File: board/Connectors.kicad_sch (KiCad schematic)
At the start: 8 parts, among them J10 Bus_Hydra_8bit, J11 Bus_Hydra_8bit, J12 Bus_Hydra_8bit, J13 Bus_Hydra_8bit, J14 Bus_Hydra_8bit, J15 Bus_Hydra_8bit, J16 Bus_Hydra_8bit, J9 Bus_Hydra_8bit

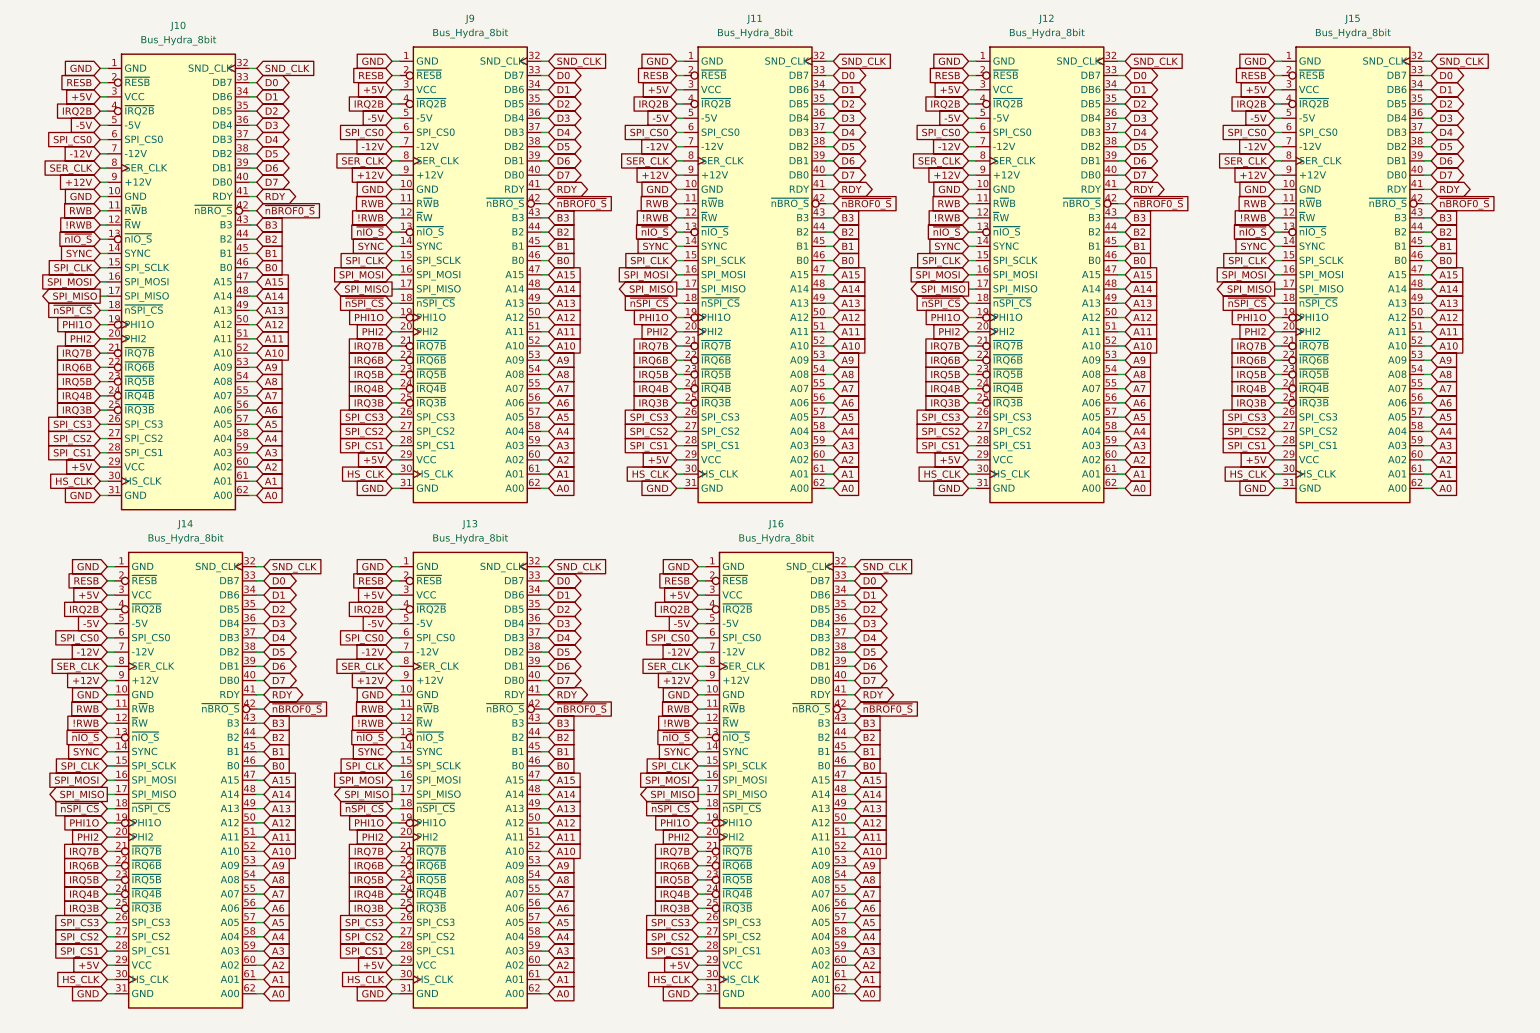
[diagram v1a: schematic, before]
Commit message: Added surface mount version of memory daughter cards, and lots of schematic updates and fixes, including adding dedicated registers for shared memory bank select at $FFF1 and IRQ vTable entry selector at $FFF2 along with the IRQ vTable registers and priority encoders for 16 IRQs
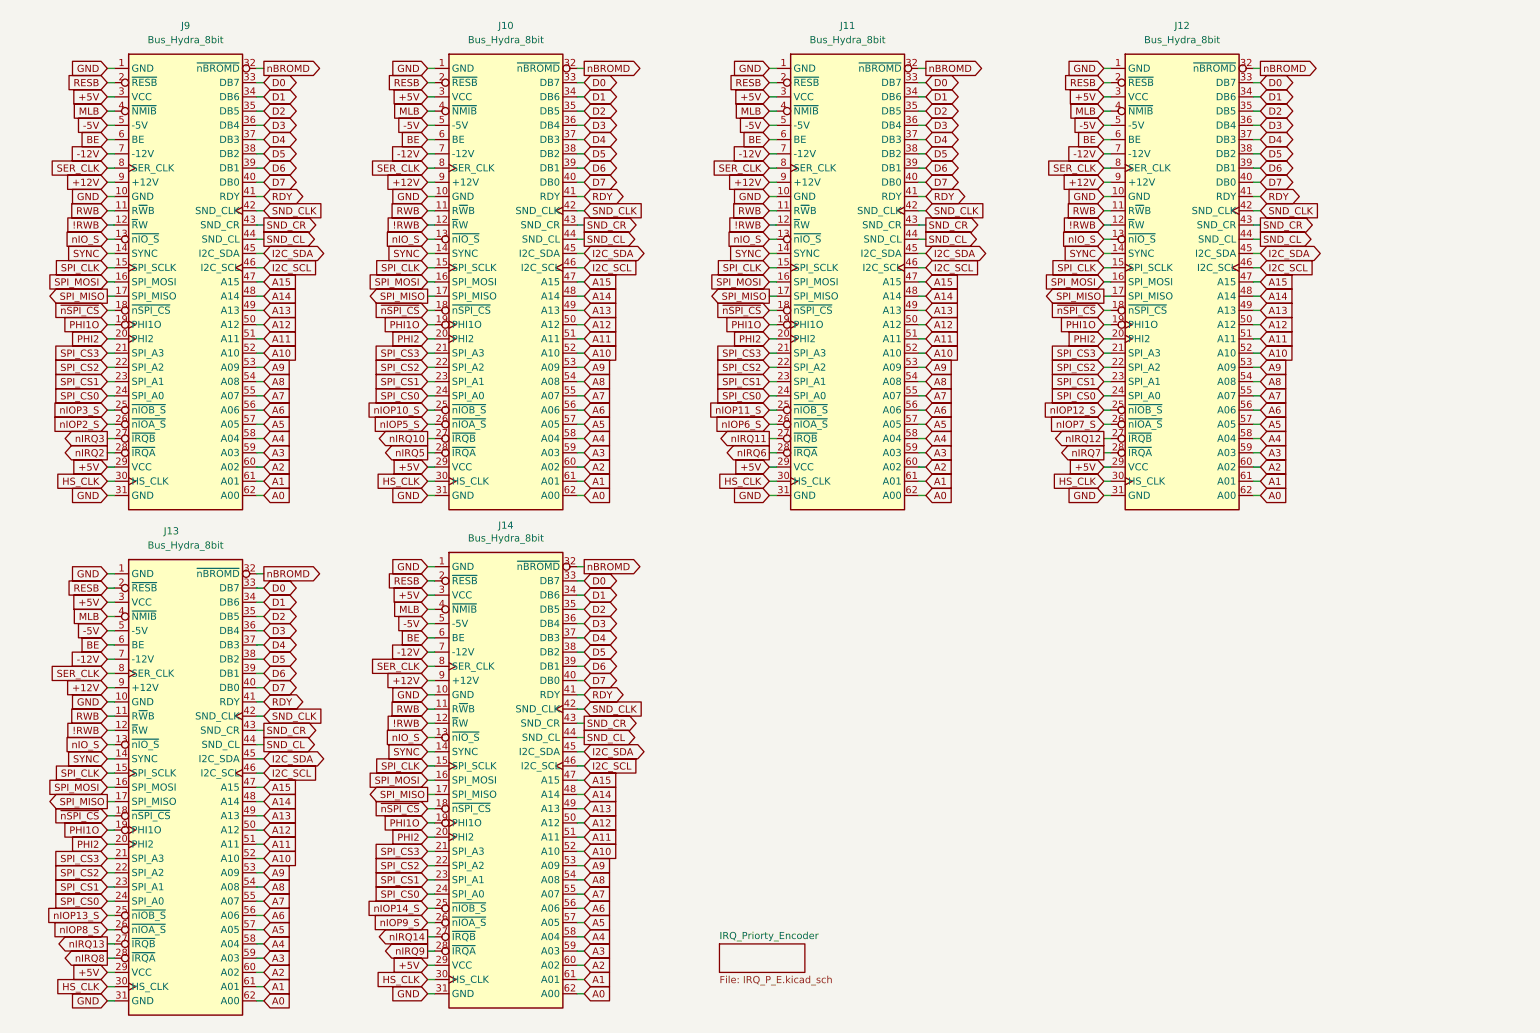
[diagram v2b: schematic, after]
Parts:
- removed J15, J16: Bus_Hydra_8bit, PC Edge:TE_7-5530843-0, symbol Connector:Bus_Hydra_8bit
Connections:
- net IRQ4B is gone; now on net SPI_CS0: J10.24 (SPI_A0), J11.24 (SPI_A0), J12.24 (SPI_A0), J13.24 (SPI_A0), J14.24 (SPI_A0), J9.24 (SPI_A0)
- net IRQ5B is gone; now on net SPI_CS1: J10.23 (SPI_A1), J11.23 (SPI_A1), J12.23 (SPI_A1), J13.23 (SPI_A1), J14.23 (SPI_A1), J9.23 (SPI_A1)
- net IRQ6B is gone; now on net SPI_CS2: J10.22 (SPI_A2), J11.22 (SPI_A2), J12.22 (SPI_A2), J13.22 (SPI_A2), J14.22 (SPI_A2), J9.22 (SPI_A2)
- net IRQ7B is gone; now on net SPI_CS3: J10.21 (SPI_A3), J11.21 (SPI_A3), J12.21 (SPI_A3), J13.21 (SPI_A3), J14.21 (SPI_A3), J9.21 (SPI_A3)
- net ~{nBROF0_S} is gone; now on net SND_CLK: J10.42 (SND_CLK), J11.42 (SND_CLK), J12.42 (SND_CLK), J13.42 (SND_CLK), J14.42 (SND_CLK), J9.42 (SND_CLK)
- net SND_CLK: no longer J10.32 (SND_CLK), J11.32 (SND_CLK), J12.32 (SND_CLK), J13.32 (SND_CLK), J14.32 (SND_CLK), J9.32 (SND_CLK)
- net SPI_CS0: no longer J10.6 (SPI_CS0), J11.6 (SPI_CS0), J12.6 (SPI_CS0), J13.6 (SPI_CS0), J14.6 (SPI_CS0), J9.6 (SPI_CS0)
- net SPI_CS1: no longer J10.28 (SPI_CS1), J11.28 (SPI_CS1), J12.28 (SPI_CS1), J13.28 (SPI_CS1), J14.28 (SPI_CS1), J9.28 (SPI_CS1)
- net SPI_CS2: no longer J10.27 (SPI_CS2), J11.27 (SPI_CS2), J12.27 (SPI_CS2), J13.27 (SPI_CS2), J14.27 (SPI_CS2), J9.27 (SPI_CS2)
- net SPI_CS3: no longer J10.26 (SPI_CS3), J11.26 (SPI_CS3), J12.26 (SPI_CS3), J13.26 (SPI_CS3), J14.26 (SPI_CS3), J9.26 (SPI_CS3)
- net B0 renamed I2C_SCL
- net B1 renamed I2C_SDA
- net B2 renamed SND_CL
- net B3 renamed SND_CR
- net IRQ2B renamed MLB
- removed net IRQ3B: J10.25 (~{IRQ3B}), J11.25 (~{IRQ3B}), J12.25 (~{IRQ3B}), J13.25 (~{IRQ3B}), J14.25 (~{IRQ3B}), J9.25 (~{IRQ3B})
- net ~{nIO_S} renamed nIO_S
- new net BE: J10.6 (BE), J11.6 (BE), J12.6 (BE), J13.6 (BE), J14.6 (BE), J9.6 (BE)
- new net nBROMD: J10.32 (~{nBROMD}), J11.32 (~{nBROMD}), J12.32 (~{nBROMD}), J13.32 (~{nBROMD}), J14.32 (~{nBROMD}), J9.32 (~{nBROMD})
- new net nIOP10_S: J10.25 (~{nIOB_S})
- new net nIOP11_S: J11.25 (~{nIOB_S})
- new net nIOP12_S: J12.25 (~{nIOB_S})
- new net nIOP13_S: J13.25 (~{nIOB_S})
- new net nIOP14_S: J14.25 (~{nIOB_S})
- new net nIOP2_S: J9.26 (~{nIOA_S})
- new net nIOP3_S: J9.25 (~{nIOB_S})
- new net nIOP5_S: J10.26 (~{nIOA_S})
- new net nIOP6_S: J11.26 (~{nIOA_S})
- new net nIOP7_S: J12.26 (~{nIOA_S})
- new net nIOP8_S: J13.26 (~{nIOA_S})
- new net nIOP9_S: J14.26 (~{nIOA_S})
- new net nIRQ10: J10.27 (~{IRQB})
- new net nIRQ11: J11.27 (~{IRQB})
- new net nIRQ12: J12.27 (~{IRQB})
- new net nIRQ13: J13.27 (~{IRQB})
- new net nIRQ14: J14.27 (~{IRQB})
- new net nIRQ2: J9.28 (~{IRQA})
- new net nIRQ3: J9.27 (~{IRQB})
- new net nIRQ5: J10.28 (~{IRQA})
- new net nIRQ6: J11.28 (~{IRQA})
- new net nIRQ7: J12.28 (~{IRQA})
- new net nIRQ8: J13.28 (~{IRQA})
- new net nIRQ9: J14.28 (~{IRQA})
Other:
- added sheet IRQ_Priorty_Encoder (IRQ_P_E.kicad_sch)

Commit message: More main PCB updates.  Rearranged some things.  Bypass caps near PS connector.  Moved front panel connector to opposite side of board.
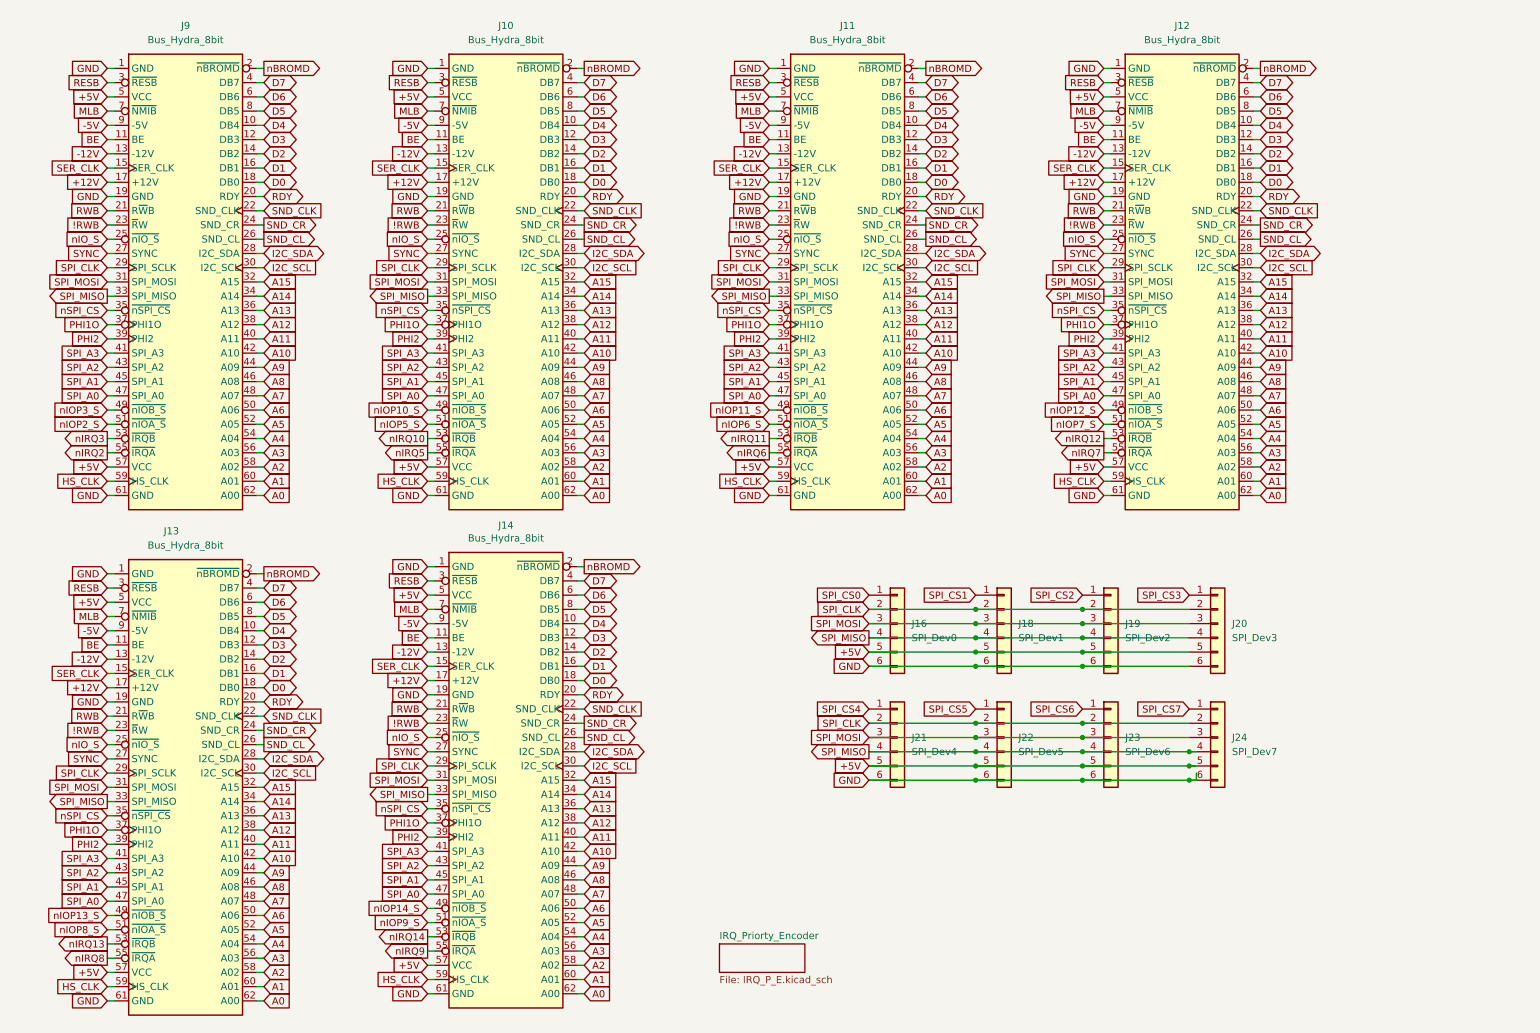
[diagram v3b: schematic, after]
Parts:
- added J16: SPI_Dev0, Connector_PinSocket_2.54mm:PinSocket_1x06_P2.54mm_Vertical, symbol Connector_Generic:Conn_01x06
- added J18: SPI_Dev1, Connector_PinSocket_2.54mm:PinSocket_1x06_P2.54mm_Vertical, symbol Connector_Generic:Conn_01x06
- added J19: SPI_Dev2, Connector_PinSocket_2.54mm:PinSocket_1x06_P2.54mm_Vertical, symbol Connector_Generic:Conn_01x06
- added J20: SPI_Dev3, Connector_PinSocket_2.54mm:PinSocket_1x06_P2.54mm_Vertical, symbol Connector_Generic:Conn_01x06
- added J21: SPI_Dev4, Connector_PinSocket_2.54mm:PinSocket_1x06_P2.54mm_Vertical, symbol Connector_Generic:Conn_01x06
- added J22: SPI_Dev5, Connector_PinSocket_2.54mm:PinSocket_1x06_P2.54mm_Vertical, symbol Connector_Generic:Conn_01x06
- added J23: SPI_Dev6, Connector_PinSocket_2.54mm:PinSocket_1x06_P2.54mm_Vertical, symbol Connector_Generic:Conn_01x06
- added J24: SPI_Dev7, Connector_PinSocket_2.54mm:PinSocket_1x06_P2.54mm_Vertical, symbol Connector_Generic:Conn_01x06
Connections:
- net ~{nSPI_CS} is gone; now on net D0: J10.18 (DB0), J11.18 (DB0), J12.18 (DB0), J13.18 (DB0), J14.18 (DB0), J9.18 (DB0)
- net !RWB: now also J10.23 (~{R}W), J11.23 (~{R}W), J12.23 (~{R}W), J13.23 (~{R}W), J14.23 (~{R}W), J9.23 (~{R}W); no longer J10.12 (~{R}W), J11.12 (~{R}W), J12.12 (~{R}W), J13.12 (~{R}W), J14.12 (~{R}W), J9.12 (~{R}W)
- net +12V: now also J10.17 (+12V), J11.17 (+12V), J12.17 (+12V), J13.17 (+12V), J14.17 (+12V), J9.17 (+12V); no longer J10.9 (+12V), J11.9 (+12V), J12.9 (+12V), J13.9 (+12V), J14.9 (+12V), J9.9 (+12V)
- net +5V: now also J10.5 (VCC), J10.57 (VCC), J11.5 (VCC), J11.57 (VCC), J12.5 (VCC), J12.57 (VCC), J13.5 (VCC), J13.57 (VCC), J14.5 (VCC), J14.57 (VCC), J9.5 (VCC), J9.57 (VCC), J16.5 (Pin_5), J18.5 (Pin_5), J19.5 (Pin_5), J20.5 (Pin_5), J21.5 (Pin_5), J22.5 (Pin_5), J23.5 (Pin_5), J24.5 (Pin_5); no longer J10.29 (VCC), J10.3 (VCC), J11.29 (VCC), J11.3 (VCC), J12.29 (VCC), J12.3 (VCC), J13.29 (VCC), J13.3 (VCC), J14.29 (VCC), J14.3 (VCC), J9.29 (VCC), J9.3 (VCC)
- net -12V: now also J10.13 (-12V), J11.13 (-12V), J12.13 (-12V), J13.13 (-12V), J14.13 (-12V), J9.13 (-12V); no longer J10.7 (-12V), J11.7 (-12V), J12.7 (-12V), J13.7 (-12V), J14.7 (-12V), J9.7 (-12V)
- net -5V: now also J10.9 (-5V), J11.9 (-5V), J12.9 (-5V), J13.9 (-5V), J14.9 (-5V), J9.9 (-5V); no longer J10.5 (-5V), J11.5 (-5V), J12.5 (-5V), J13.5 (-5V), J14.5 (-5V), J9.5 (-5V)
- net A1: now also J10.60 (A01), J11.60 (A01), J12.60 (A01), J13.60 (A01), J14.60 (A01), J9.60 (A01); no longer J10.61 (A01), J11.61 (A01), J12.61 (A01), J13.61 (A01), J14.61 (A01), J9.61 (A01)
- net A10: now also J10.42 (A10), J11.42 (A10), J12.42 (A10), J13.42 (A10), J14.42 (A10), J9.42 (A10); no longer J10.52 (A10), J11.52 (A10), J12.52 (A10), J13.52 (A10), J14.52 (A10), J9.52 (A10)
- net A11: now also J10.40 (A11), J11.40 (A11), J12.40 (A11), J13.40 (A11), J14.40 (A11), J9.40 (A11); no longer J10.51 (A11), J11.51 (A11), J12.51 (A11), J13.51 (A11), J14.51 (A11), J9.51 (A11)
- net A12: now also J10.38 (A12), J11.38 (A12), J12.38 (A12), J13.38 (A12), J14.38 (A12), J9.38 (A12); no longer J10.50 (A12), J11.50 (A12), J12.50 (A12), J13.50 (A12), J14.50 (A12), J9.50 (A12)
- net A13: now also J10.36 (A13), J11.36 (A13), J12.36 (A13), J13.36 (A13), J14.36 (A13), J9.36 (A13); no longer J10.49 (A13), J11.49 (A13), J12.49 (A13), J13.49 (A13), J14.49 (A13), J9.49 (A13)
- net A14: now also J10.34 (A14), J11.34 (A14), J12.34 (A14), J13.34 (A14), J14.34 (A14), J9.34 (A14); no longer J10.48 (A14), J11.48 (A14), J12.48 (A14), J13.48 (A14), J14.48 (A14), J9.48 (A14)
- net A15: now also J10.32 (A15), J11.32 (A15), J12.32 (A15), J13.32 (A15), J14.32 (A15), J9.32 (A15); no longer J10.47 (A15), J11.47 (A15), J12.47 (A15), J13.47 (A15), J14.47 (A15), J9.47 (A15)
- net A2: now also J10.58 (A02), J11.58 (A02), J12.58 (A02), J13.58 (A02), J14.58 (A02), J9.58 (A02); no longer J10.60 (A02), J11.60 (A02), J12.60 (A02), J13.60 (A02), J14.60 (A02), J9.60 (A02)
- net A3: now also J10.56 (A03), J11.56 (A03), J12.56 (A03), J13.56 (A03), J14.56 (A03), J9.56 (A03); no longer J10.59 (A03), J11.59 (A03), J12.59 (A03), J13.59 (A03), J14.59 (A03), J9.59 (A03)
- net A4: now also J10.54 (A04), J11.54 (A04), J12.54 (A04), J13.54 (A04), J14.54 (A04), J9.54 (A04); no longer J10.58 (A04), J11.58 (A04), J12.58 (A04), J13.58 (A04), J14.58 (A04), J9.58 (A04)
- net A5: now also J10.52 (A05), J11.52 (A05), J12.52 (A05), J13.52 (A05), J14.52 (A05), J9.52 (A05); no longer J10.57 (A05), J11.57 (A05), J12.57 (A05), J13.57 (A05), J14.57 (A05), J9.57 (A05)
- net A6: now also J10.50 (A06), J11.50 (A06), J12.50 (A06), J13.50 (A06), J14.50 (A06), J9.50 (A06); no longer J10.56 (A06), J11.56 (A06), J12.56 (A06), J13.56 (A06), J14.56 (A06), J9.56 (A06)
- net A7: now also J10.48 (A07), J11.48 (A07), J12.48 (A07), J13.48 (A07), J14.48 (A07), J9.48 (A07); no longer J10.55 (A07), J11.55 (A07), J12.55 (A07), J13.55 (A07), J14.55 (A07), J9.55 (A07)
- net A8: now also J10.46 (A08), J11.46 (A08), J12.46 (A08), J13.46 (A08), J14.46 (A08), J9.46 (A08); no longer J10.54 (A08), J11.54 (A08), J12.54 (A08), J13.54 (A08), J14.54 (A08), J9.54 (A08)
- net A9: now also J10.44 (A09), J11.44 (A09), J12.44 (A09), J13.44 (A09), J14.44 (A09), J9.44 (A09); no longer J10.53 (A09), J11.53 (A09), J12.53 (A09), J13.53 (A09), J14.53 (A09), J9.53 (A09)
- net BE: now also J10.11 (BE), J11.11 (BE), J12.11 (BE), J13.11 (BE), J14.11 (BE), J9.11 (BE); no longer J10.6 (BE), J11.6 (BE), J12.6 (BE), J13.6 (BE), J14.6 (BE), J9.6 (BE)
- net D0: no longer J10.33 (DB7), J11.33 (DB7), J12.33 (DB7), J13.33 (DB7), J14.33 (DB7), J9.33 (DB7)
- net D1: now also J10.16 (DB1), J11.16 (DB1), J12.16 (DB1), J13.16 (DB1), J14.16 (DB1), J9.16 (DB1); no longer J10.34 (DB6), J11.34 (DB6), J12.34 (DB6), J13.34 (DB6), J14.34 (DB6), J9.34 (DB6)
- net D2: now also J10.14 (DB2), J11.14 (DB2), J12.14 (DB2), J13.14 (DB2), J14.14 (DB2), J9.14 (DB2); no longer J10.35 (DB5), J11.35 (DB5), J12.35 (DB5), J13.35 (DB5), J14.35 (DB5), J9.35 (DB5)
- net D3: now also J10.12 (DB3), J11.12 (DB3), J12.12 (DB3), J13.12 (DB3), J14.12 (DB3), J9.12 (DB3); no longer J10.36 (DB4), J11.36 (DB4), J12.36 (DB4), J13.36 (DB4), J14.36 (DB4), J9.36 (DB4)
- net D4: now also J10.10 (DB4), J11.10 (DB4), J12.10 (DB4), J13.10 (DB4), J14.10 (DB4), J9.10 (DB4); no longer J10.37 (DB3), J11.37 (DB3), J12.37 (DB3), J13.37 (DB3), J14.37 (DB3), J9.37 (DB3)
- net D5: now also J10.8 (DB5), J11.8 (DB5), J12.8 (DB5), J13.8 (DB5), J14.8 (DB5), J9.8 (DB5); no longer J10.38 (DB2), J11.38 (DB2), J12.38 (DB2), J13.38 (DB2), J14.38 (DB2), J9.38 (DB2)
- net D6: now also J10.6 (DB6), J11.6 (DB6), J12.6 (DB6), J13.6 (DB6), J14.6 (DB6), J9.6 (DB6); no longer J10.39 (DB1), J11.39 (DB1), J12.39 (DB1), J13.39 (DB1), J14.39 (DB1), J9.39 (DB1)
- net D7: now also J10.4 (DB7), J11.4 (DB7), J12.4 (DB7), J13.4 (DB7), J14.4 (DB7), J9.4 (DB7); no longer J10.40 (DB0), J11.40 (DB0), J12.40 (DB0), J13.40 (DB0), J14.40 (DB0), J9.40 (DB0)
- net GND: now also J10.19 (GND), J10.61 (GND), J11.19 (GND), J11.61 (GND), J12.19 (GND), J12.61 (GND), J13.19 (GND), J13.61 (GND), J14.19 (GND), J14.61 (GND), J9.19 (GND), J9.61 (GND), J16.6 (Pin_6), J18.6 (Pin_6), J19.6 (Pin_6), J20.6 (Pin_6), J21.6 (Pin_6), J22.6 (Pin_6), J23.6 (Pin_6), J24.6 (Pin_6); no longer J10.10 (GND), J10.31 (GND), J11.10 (GND), J11.31 (GND), J12.10 (GND), J12.31 (GND), J13.10 (GND), J13.31 (GND), J14.10 (GND), J14.31 (GND), J9.10 (GND), J9.31 (GND)
- net HS_CLK: now also J10.59 (HS_CLK), J11.59 (HS_CLK), J12.59 (HS_CLK), J13.59 (HS_CLK), J14.59 (HS_CLK), J9.59 (HS_CLK); no longer J10.30 (HS_CLK), J11.30 (HS_CLK), J12.30 (HS_CLK), J13.30 (HS_CLK), J14.30 (HS_CLK), J9.30 (HS_CLK)
- net I2C_SCL: now also J10.30 (I2C_SCL), J11.30 (I2C_SCL), J12.30 (I2C_SCL), J13.30 (I2C_SCL), J14.30 (I2C_SCL), J9.30 (I2C_SCL); no longer J10.46 (I2C_SCL), J11.46 (I2C_SCL), J12.46 (I2C_SCL), J13.46 (I2C_SCL), J14.46 (I2C_SCL), J9.46 (I2C_SCL)
- net I2C_SDA: now also J10.28 (I2C_SDA), J11.28 (I2C_SDA), J12.28 (I2C_SDA), J13.28 (I2C_SDA), J14.28 (I2C_SDA), J9.28 (I2C_SDA); no longer J10.45 (I2C_SDA), J11.45 (I2C_SDA), J12.45 (I2C_SDA), J13.45 (I2C_SDA), J14.45 (I2C_SDA), J9.45 (I2C_SDA)
- net MLB: now also J10.7 (~{NMIB}), J11.7 (~{NMIB}), J12.7 (~{NMIB}), J13.7 (~{NMIB}), J14.7 (~{NMIB}), J9.7 (~{NMIB}); no longer J10.4 (~{NMIB}), J11.4 (~{NMIB}), J12.4 (~{NMIB}), J13.4 (~{NMIB}), J14.4 (~{NMIB}), J9.4 (~{NMIB})
- net PHI1O: now also J10.37 (PHI1O), J11.37 (PHI1O), J12.37 (PHI1O), J13.37 (PHI1O), J14.37 (PHI1O), J9.37 (PHI1O); no longer J10.19 (PHI1O), J11.19 (PHI1O), J12.19 (PHI1O), J13.19 (PHI1O), J14.19 (PHI1O), J9.19 (PHI1O)
- net PHI2: now also J10.39 (PHI2), J11.39 (PHI2), J12.39 (PHI2), J13.39 (PHI2), J14.39 (PHI2), J9.39 (PHI2); no longer J10.20 (PHI2), J11.20 (PHI2), J12.20 (PHI2), J13.20 (PHI2), J14.20 (PHI2), J9.20 (PHI2)
- net RDY: now also J10.20 (RDY), J11.20 (RDY), J12.20 (RDY), J13.20 (RDY), J14.20 (RDY), J9.20 (RDY); no longer J10.41 (RDY), J11.41 (RDY), J12.41 (RDY), J13.41 (RDY), J14.41 (RDY), J9.41 (RDY)
- net RESB: now also J10.3 (~{RESB}), J11.3 (~{RESB}), J12.3 (~{RESB}), J13.3 (~{RESB}), J14.3 (~{RESB}), J9.3 (~{RESB}); no longer J10.2 (~{RESB}), J11.2 (~{RESB}), J12.2 (~{RESB}), J13.2 (~{RESB}), J14.2 (~{RESB}), J9.2 (~{RESB})
- net RWB: now also J10.21 (R~{W}B), J11.21 (R~{W}B), J12.21 (R~{W}B), J13.21 (R~{W}B), J14.21 (R~{W}B), J9.21 (R~{W}B); no longer J10.11 (R~{W}B), J11.11 (R~{W}B), J12.11 (R~{W}B), J13.11 (R~{W}B), J14.11 (R~{W}B), J9.11 (R~{W}B)
- net SER_CLK: now also J10.15 (SER_CLK), J11.15 (SER_CLK), J12.15 (SER_CLK), J13.15 (SER_CLK), J14.15 (SER_CLK), J9.15 (SER_CLK); no longer J10.8 (SER_CLK), J11.8 (SER_CLK), J12.8 (SER_CLK), J13.8 (SER_CLK), J14.8 (SER_CLK), J9.8 (SER_CLK)
- net SND_CL: now also J10.26 (SND_CL), J11.26 (SND_CL), J12.26 (SND_CL), J13.26 (SND_CL), J14.26 (SND_CL), J9.26 (SND_CL); no longer J10.44 (SND_CL), J11.44 (SND_CL), J12.44 (SND_CL), J13.44 (SND_CL), J14.44 (SND_CL), J9.44 (SND_CL)
- net SND_CLK: now also J10.22 (SND_CLK), J11.22 (SND_CLK), J12.22 (SND_CLK), J13.22 (SND_CLK), J14.22 (SND_CLK), J9.22 (SND_CLK); no longer J10.42 (SND_CLK), J11.42 (SND_CLK), J12.42 (SND_CLK), J13.42 (SND_CLK), J14.42 (SND_CLK), J9.42 (SND_CLK)
- net SND_CR: now also J10.24 (SND_CR), J11.24 (SND_CR), J12.24 (SND_CR), J13.24 (SND_CR), J14.24 (SND_CR), J9.24 (SND_CR); no longer J10.43 (SND_CR), J11.43 (SND_CR), J12.43 (SND_CR), J13.43 (SND_CR), J14.43 (SND_CR), J9.43 (SND_CR)
- net SPI_CLK: now also J10.29 (SPI_SCLK), J11.29 (SPI_SCLK), J12.29 (SPI_SCLK), J13.29 (SPI_SCLK), J14.29 (SPI_SCLK), J9.29 (SPI_SCLK), J16.2 (Pin_2), J18.2 (Pin_2), J19.2 (Pin_2), J20.2 (Pin_2), J21.2 (Pin_2), J22.2 (Pin_2), J23.2 (Pin_2), J24.2 (Pin_2); no longer J10.15 (SPI_SCLK), J11.15 (SPI_SCLK), J12.15 (SPI_SCLK), J13.15 (SPI_SCLK), J14.15 (SPI_SCLK), J9.15 (SPI_SCLK)
- net SPI_CS0: now also J16.1 (Pin_1); no longer J10.24 (SPI_A0), J11.24 (SPI_A0), J12.24 (SPI_A0), J13.24 (SPI_A0), J14.24 (SPI_A0), J9.24 (SPI_A0)
- net SPI_CS1: now also J18.1 (Pin_1); no longer J10.23 (SPI_A1), J11.23 (SPI_A1), J12.23 (SPI_A1), J13.23 (SPI_A1), J14.23 (SPI_A1), J9.23 (SPI_A1)
- net SPI_CS2: now also J19.1 (Pin_1); no longer J10.22 (SPI_A2), J11.22 (SPI_A2), J12.22 (SPI_A2), J13.22 (SPI_A2), J14.22 (SPI_A2), J9.22 (SPI_A2)
- net SPI_CS3: now also J20.1 (Pin_1); no longer J10.21 (SPI_A3), J11.21 (SPI_A3), J12.21 (SPI_A3), J13.21 (SPI_A3), J14.21 (SPI_A3), J9.21 (SPI_A3)
- net SPI_MISO: now also J10.33 (SPI_MISO), J11.33 (SPI_MISO), J12.33 (SPI_MISO), J13.33 (SPI_MISO), J14.33 (SPI_MISO), J9.33 (SPI_MISO), J16.4 (Pin_4), J18.4 (Pin_4), J19.4 (Pin_4), J20.4 (Pin_4), J21.4 (Pin_4), J22.4 (Pin_4), J23.4 (Pin_4), J24.4 (Pin_4); no longer J10.17 (SPI_MISO), J11.17 (SPI_MISO), J12.17 (SPI_MISO), J13.17 (SPI_MISO), J14.17 (SPI_MISO), J9.17 (SPI_MISO)
- net SPI_MOSI: now also J10.31 (SPI_MOSI), J11.31 (SPI_MOSI), J12.31 (SPI_MOSI), J13.31 (SPI_MOSI), J14.31 (SPI_MOSI), J9.31 (SPI_MOSI), J16.3 (Pin_3), J18.3 (Pin_3), J19.3 (Pin_3), J20.3 (Pin_3), J21.3 (Pin_3), J22.3 (Pin_3), J23.3 (Pin_3), J24.3 (Pin_3); no longer J10.16 (SPI_MOSI), J11.16 (SPI_MOSI), J12.16 (SPI_MOSI), J13.16 (SPI_MOSI), J14.16 (SPI_MOSI), J9.16 (SPI_MOSI)
- net SYNC: now also J10.27 (SYNC), J11.27 (SYNC), J12.27 (SYNC), J13.27 (SYNC), J14.27 (SYNC), J9.27 (SYNC); no longer J10.14 (SYNC), J11.14 (SYNC), J12.14 (SYNC), J13.14 (SYNC), J14.14 (SYNC), J9.14 (SYNC)
- net nBROMD: now also J10.2 (~{nBROMD}), J11.2 (~{nBROMD}), J12.2 (~{nBROMD}), J13.2 (~{nBROMD}), J14.2 (~{nBROMD}), J9.2 (~{nBROMD}); no longer J10.32 (~{nBROMD}), J11.32 (~{nBROMD}), J12.32 (~{nBROMD}), J13.32 (~{nBROMD}), J14.32 (~{nBROMD}), J9.32 (~{nBROMD})
- net nIOP10_S: now also J10.49 (~{nIOB_S}); no longer J10.25 (~{nIOB_S})
- net nIOP11_S: now also J11.49 (~{nIOB_S}); no longer J11.25 (~{nIOB_S})
- net nIOP12_S: now also J12.49 (~{nIOB_S}); no longer J12.25 (~{nIOB_S})
- net nIOP13_S: now also J13.49 (~{nIOB_S}); no longer J13.25 (~{nIOB_S})
- net nIOP14_S: now also J14.49 (~{nIOB_S}); no longer J14.25 (~{nIOB_S})
- net nIOP2_S: now also J9.51 (~{nIOA_S}); no longer J9.26 (~{nIOA_S})
- net nIOP3_S: now also J9.49 (~{nIOB_S}); no longer J9.25 (~{nIOB_S})
- net nIOP5_S: now also J10.51 (~{nIOA_S}); no longer J10.26 (~{nIOA_S})
- net nIOP6_S: now also J11.51 (~{nIOA_S}); no longer J11.26 (~{nIOA_S})
- net nIOP7_S: now also J12.51 (~{nIOA_S}); no longer J12.26 (~{nIOA_S})
- net nIOP8_S: now also J13.51 (~{nIOA_S}); no longer J13.26 (~{nIOA_S})
- net nIOP9_S: now also J14.51 (~{nIOA_S}); no longer J14.26 (~{nIOA_S})
- net nIO_S: now also J10.25 (~{nIO_S}), J11.25 (~{nIO_S}), J12.25 (~{nIO_S}), J13.25 (~{nIO_S}), J14.25 (~{nIO_S}), J9.25 (~{nIO_S}); no longer J10.13 (~{nIO_S}), J11.13 (~{nIO_S}), J12.13 (~{nIO_S}), J13.13 (~{nIO_S}), J14.13 (~{nIO_S}), J9.13 (~{nIO_S})
- net nIRQ10: now also J10.53 (~{IRQB}); no longer J10.27 (~{IRQB})
- net nIRQ11: now also J11.53 (~{IRQB}); no longer J11.27 (~{IRQB})
- net nIRQ12: now also J12.53 (~{IRQB}); no longer J12.27 (~{IRQB})
- net nIRQ13: now also J13.53 (~{IRQB}); no longer J13.27 (~{IRQB})
- net nIRQ14: now also J14.53 (~{IRQB}); no longer J14.27 (~{IRQB})
- net nIRQ2: now also J9.55 (~{IRQA}); no longer J9.28 (~{IRQA})
- net nIRQ3: now also J9.53 (~{IRQB}); no longer J9.27 (~{IRQB})
- net nIRQ5: now also J10.55 (~{IRQA}); no longer J10.28 (~{IRQA})
- net nIRQ6: now also J11.55 (~{IRQA}); no longer J11.28 (~{IRQA})
- net nIRQ7: now also J12.55 (~{IRQA}); no longer J12.28 (~{IRQA})
- net nIRQ8: now also J13.55 (~{IRQA}); no longer J13.28 (~{IRQA})
- net nIRQ9: now also J14.55 (~{IRQA}); no longer J14.28 (~{IRQA})
- new net SPI_A0: J10.47 (SPI_A0), J11.47 (SPI_A0), J12.47 (SPI_A0), J13.47 (SPI_A0), J14.47 (SPI_A0), J9.47 (SPI_A0)
- new net SPI_A1: J10.45 (SPI_A1), J11.45 (SPI_A1), J12.45 (SPI_A1), J13.45 (SPI_A1), J14.45 (SPI_A1), J9.45 (SPI_A1)
- new net SPI_A2: J10.43 (SPI_A2), J11.43 (SPI_A2), J12.43 (SPI_A2), J13.43 (SPI_A2), J14.43 (SPI_A2), J9.43 (SPI_A2)
- new net SPI_A3: J10.41 (SPI_A3), J11.41 (SPI_A3), J12.41 (SPI_A3), J13.41 (SPI_A3), J14.41 (SPI_A3), J9.41 (SPI_A3)
- new net SPI_CS4: J21.1 (Pin_1)
- new net SPI_CS5: J22.1 (Pin_1)
- new net SPI_CS6: J23.1 (Pin_1)
- new net SPI_CS7: J24.1 (Pin_1)
- new net nSPI_CS: J10.35 (~{nSPI_CS}), J11.35 (~{nSPI_CS}), J12.35 (~{nSPI_CS}), J13.35 (~{nSPI_CS}), J14.35 (~{nSPI_CS}), J9.35 (~{nSPI_CS})
